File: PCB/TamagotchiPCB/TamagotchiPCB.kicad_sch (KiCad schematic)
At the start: 9 parts, among them U1 ESP32_DevKit_V1_DOIT

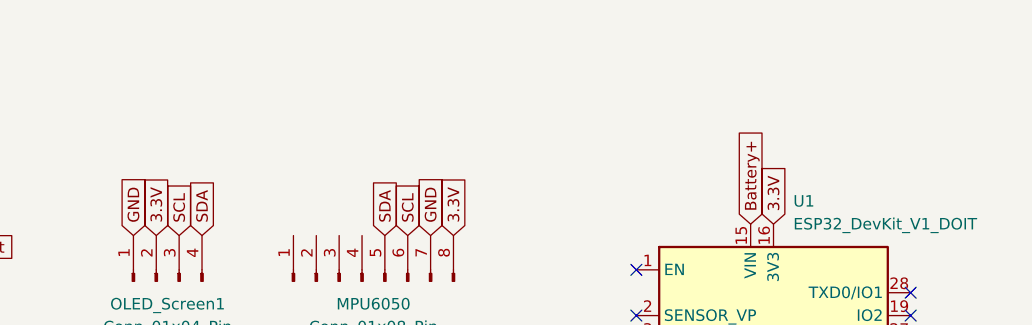
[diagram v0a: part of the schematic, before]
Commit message: edit pcb imagenes
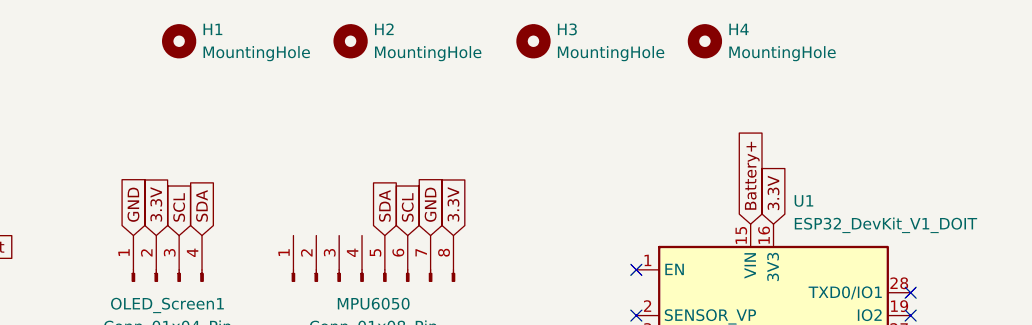
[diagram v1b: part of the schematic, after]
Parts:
- added H1, H2, H3, H4: MountingHole, MountingHole:MountingHole_3mm, symbol Mechanical:MountingHole
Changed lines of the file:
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@@
+    )
+  )
+  (symbol (lib_id "Mechanical:MountingHole") (at 219.71 57.15 0) (unit 1)
+    (in_bom yes) (on_board yes) (dnp no) (fields_autoplaced)
+    (property "Reference" "H3" (at 222.25 55.88 0)
+      (effects (font (size 1.27 1.27)) (justify left))
+    )
+    (property "Value" "MountingHole" (at 222.25 58.42 0)
+      (effects (font (size 1.27 1.27)) (justify left))
+    )
+    (property "Footprint" "MountingHole:MountingHole_3mm" (at 219.71 57.15 0)
+      (effects (font (size 1.27 1.27)) hide)
+    )
+    (property "Datasheet" "~" (at 219.71 57.15 0)
+      (effects (font (size 1.27 1.27)) hide)
+    )
+    (instances
+      (project "TamagotchiPCB"
+        (path "/ffc02a99-2910-4f6e-b90e-b40abf058a2e"
+          (reference "H3") (unit 1)
+        )
+      )
     )
   )
@@
         (path "/ffc02a99-2910-4f6e-b90e-b40abf058a2e"
           (reference "OLED_Screen1") (unit 1)
+        )
+      )
+    )
+  )
+  (symbol (lib_id "Mechanical:MountingHole") (at 238.76 57.15 0) (unit 1)
+    (in_bom yes) (on_board yes) (dnp no) (fields_autoplaced)
+    (property "Reference" "H4" (at 241.3 55.88 0)
+      (effects (font (size 1.27 1.27)) (justify left))
+    )
+    (property "Value" "MountingHole" (at 241.3 58.42 0)
+      (effects (font (size 1.27 1.27)) (justify left))
+    )
+    (property "Footprint" "MountingHole:MountingHole_3mm" (at 238.76 57.15 0)
+      (effects (font (size 1.27 1.27)) hide)
+    )
+    (property "Datasheet" "~" (at 238.76 57.15 0)
+      (effects (font (size 1.27 1.27)) hide)
+    )
+    (instances
+      (project "TamagotchiPCB"
+        (path "/ffc02a99-2910-4f6e-b90e-b40abf058a2e"
+          (reference "H4") (unit 1)
         )
       )
@@
     )
   )
+  (symbol (lib_id "Mechanical:MountingHole") (at 180.34 57.15 0) (unit 1)
+    (in_bom yes) (on_board yes) (dnp no) (fields_autoplaced)
+    (property "Reference" "H1" (at 182.88 55.88 0)
+      (effects (font (size 1.27 1.27)) (justify left))
+    )
+    (property "Value" "MountingHole" (at 182.88 58.42 0)
+      (effects (font (size 1.27 1.27)) (justify left))
+    )
+    (property "Footprint" "MountingHole:MountingHole_3mm" (at 180.34 57.15 0)
+      (effects (font (size 1.27 1.27)) hide)
+    )
+    (property "Datasheet" "~" (at 180.34 57.15 0)
+      (effects (font (size 1.27 1.27)) hide)
+    )
+    (instances
+      (project "TamagotchiPCB"
+        (path "/ffc02a99-2910-4f6e-b90e-b40abf058a2e"
+          (reference "H1") (unit 1)
+        )
+      )
+    )
+  )
   (symbol (lib_name "SW_Push_Dual_1") (lib_id "Switch:SW_Push_Dual") (at 149.86 80.01 0) (unit 1)
     (in_bom yes) (on_board yes) (dnp no) (fields_autoplaced)
@@
         )
       )
+    )
+  )
+  (symbol (lib_id "Mechanical:MountingHole") (at 199.39 57.15 0) (unit 1)
+    (in_bom yes) (on_board yes) (dnp no) (fields_autoplaced)
+    (property "Reference" "H2" (at 201.93 55.88 0)
+      (effects (font (size 1.27 1.27)) (justify left))
+    )
+    (property "Value" "MountingHole" (at 201.93 58.42 0)
+      (effects (font (size 1.27 1.27)) (justify left))
+    )
+    (property "Footprint" "MountingHole:MountingHole_3mm" (at 199.39 57.15 0)
+      (effects (font (size 1.27 1.27)) hide)
+    )
+    (property "Datasheet" "~" (at 199.39 57.15 0)
+      (effects (font (size 1.27 1.27)) hide)
+    )
+    (instances
+      (project "TamagotchiPCB"
+        (path "/ffc02a99-2910-4f6e-b90e-b40abf058a2e"
+          (reference "H2") (unit 1)
+        )
+      )
